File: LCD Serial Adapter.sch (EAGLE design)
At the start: 10 parts, among them IC1 74HC595N, IC2 74LHC95N, IC3 DS1866, IC4 MAX4544, Q1 BC327

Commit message: Add files via upload
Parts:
- C1, C2: device SparkFun-Capacitors:CAPPTH2 -> 00 Nik misc:C-USSMD
- IC3: value DS1866 -> DS1866Z; device nik analog ic:DS1866 -> 00 Nik misc:DS1866Z
- IC4: device nik analog ic:MAX4544CPA -> 00 Nik misc:MAX4544CSA
- JP2: value MCU -> (none); device pinhead:PINHD-1X6 -> pinhead:PINHD-2X3
- Q1: value BC327 -> BC807; device transistor-pnp:BC327 -> 00 Nik misc:BC807
- R1: device resistor:R-US_0204/2V -> 00 Nik misc:R-USSMD
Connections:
- net +5V: now also JP2.2; no longer JP2.6
- net BL-PWM: now also JP2.4; no longer JP2.5
- net DATA: now also JP2.6; no longer JP2.4
- net GND: now also IC3P.GND, IC4P.GND, JP2.5; no longer IC3SUPPLY.GND, IC4SUPPLY.GND, JP2.1
- net LATCH: no longer JP2.2
- net SHIFT: now also JP2.1; no longer JP2.3
- net VCC: now also IC3P.VCC, IC4P.VCC; no longer IC3SUPPLY.VCC, IC4SUPPLY.VCC
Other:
- moved on the sheet: C2, IC1P, JP2

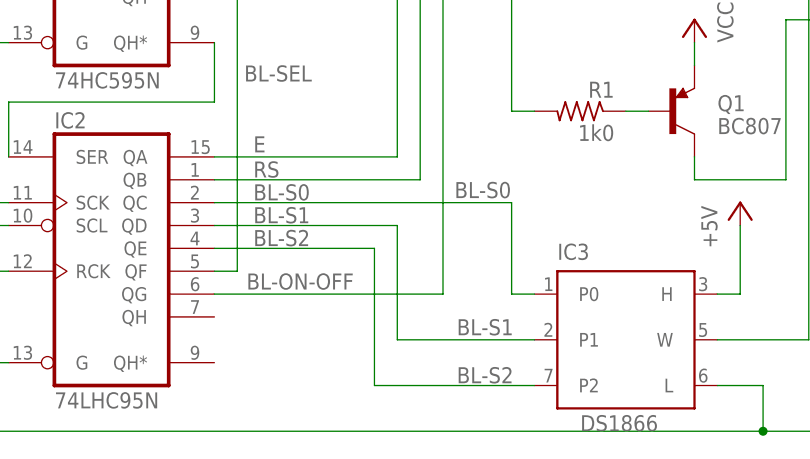
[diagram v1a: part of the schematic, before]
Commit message: Fix contrast signal names
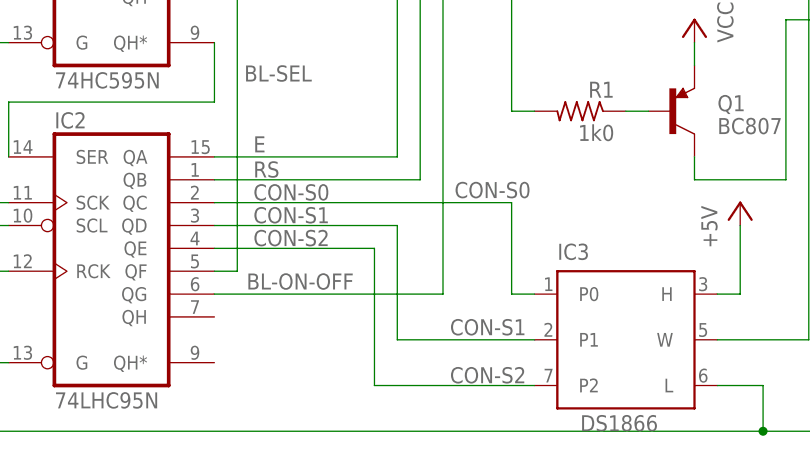
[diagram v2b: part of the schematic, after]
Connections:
- net BL-S0 renamed CON-S0
- net BL-S1 renamed CON-S1
- net BL-S2 renamed CON-S2
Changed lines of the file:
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@@
 </segment>
 </net>
-<net name="BL-S0" class="0">
+<net name="CON-S0" class="0">
 <segment>
 <pinref part="IC2" gate="A" pin="QC"/>
@@
 </segment>
 </net>
-<net name="BL-S1" class="0">
+<net name="CON-S1" class="0">
 <segment>
 <pinref part="IC2" gate="A" pin="QD"/>
@@
 <pinref part="IC3" gate="IC" pin="P1"/>
 <wire x1="134.62" y1="116.84" x2="119.38" y2="116.84" width="0.1524" layer="91"/>
-<label x="125.984" y="117.348" size="1.778" layer="95"/>
+<label x="125.222" y="117.348" size="1.778" layer="95"/>
 <label x="103.378" y="129.794" size="1.778" layer="95"/>
 </segment>
@@
 </segment>
 </net>
-<net name="BL-S2" class="0">
+<net name="CON-S2" class="0">
 <segment>
 <pinref part="IC3" gate="IC" pin="P2"/>
@@
 <pinref part="IC2" gate="A" pin="QE"/>
 <wire x1="116.84" y1="127" x2="99.06" y2="127" width="0.1524" layer="91"/>
-<label x="125.984" y="112.014" size="1.778" layer="95"/>
+<label x="125.222" y="112.014" size="1.778" layer="95"/>
 <label x="103.378" y="127.254" size="1.778" layer="95"/>
 </segment>
